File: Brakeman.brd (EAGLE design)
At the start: 37.3 x 48.3 mm, 9 parts

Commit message: added values for connectors
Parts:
- PADL1, PADL2, PADNF2, PADSF2: value (none) -> pad
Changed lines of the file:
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@@
 <attribute name="VALUE" x="18.2626" y="33.655" size="0.0254" layer="28" rot="MR0"/>
 </element>
-<element name="PADL1" library="wirepad" package="SMD1.27-2.54" value="" x="18.2626" y="33.655" smashed="yes">
+<element name="PADL1" library="wirepad" package="SMD1.27-2.54" value="pad" x="18.2626" y="33.655" smashed="yes">
 <attribute name="VALUE" x="18.2626" y="33.655" size="0.0254" layer="27"/>
 </element>
@@
 <attribute name="VALUE" x="5.8166" y="26.162" size="0.0254" layer="28" rot="MR200"/>
 </element>
-<element name="PADL2" library="wirepad" package="SMD1.27-2.54" value="" x="5.8166" y="26.162" smashed="yes" rot="R160">
+<element name="PADL2" library="wirepad" package="SMD1.27-2.54" value="pad" x="5.8166" y="26.162" smashed="yes" rot="R160">
 <attribute name="VALUE" x="5.8166" y="26.162" size="0.0254" layer="27" rot="R160"/>
 </element>
-<element name="PADNF2" library="wirepad" package="SMD1.27-2.54" value="" x="14.859" y="19.9644" smashed="yes" rot="R90">
+<element name="PADNF2" library="wirepad" package="SMD1.27-2.54" value="pad" x="14.859" y="19.9644" smashed="yes" rot="R90">
 <attribute name="VALUE" x="14.859" y="19.9644" size="0.0254" layer="27" rot="R90"/>
 </element>
-<element name="PADSF2" library="wirepad" package="SMD1.27-2.54" value="" x="8.7122" y="19.9898" smashed="yes" rot="R90">
+<element name="PADSF2" library="wirepad" package="SMD1.27-2.54" value="pad" x="8.7122" y="19.9898" smashed="yes" rot="R90">
 <attribute name="VALUE" x="8.7122" y="19.9898" size="0.0254" layer="27" rot="R90"/>
 </element>

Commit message: added values for connectors
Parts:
- PADNA, PADNA2, PADNF, PADSF: value (none) -> pad
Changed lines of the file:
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@@
 <attribute name="VALUE" x="13.4366" y="29.21" size="1.27" layer="28" rot="MR0"/>
 </element>
-<element name="PADNA" library="wirepad" package="SMD1.27-2.54" value="" x="18.2626" y="33.655" smashed="yes" rot="MR0">
+<element name="PADNA" library="wirepad" package="SMD1.27-2.54" value="pad" x="18.2626" y="33.655" smashed="yes" rot="MR0">
 <attribute name="VALUE" x="18.2626" y="33.655" size="0.0254" layer="28" rot="MR0"/>
 </element>
@@
 <attribute name="VALUE" x="18.2626" y="33.655" size="0.0254" layer="27"/>
 </element>
-<element name="PADNA2" library="wirepad" package="SMD1.27-2.54" value="" x="5.8166" y="26.162" smashed="yes" rot="MR200">
+<element name="PADNA2" library="wirepad" package="SMD1.27-2.54" value="pad" x="5.8166" y="26.162" smashed="yes" rot="MR200">
 <attribute name="VALUE" x="5.8166" y="26.162" size="0.0254" layer="28" rot="MR200"/>
 </element>
@@
 <attribute name="VALUE" x="8.7122" y="19.9898" size="0.0254" layer="27" rot="R90"/>
 </element>
-<element name="PADSF" library="wirepad" package="SMD1.27-2.54" value="" x="8.7122" y="19.9644" smashed="yes" rot="MR270">
+<element name="PADSF" library="wirepad" package="SMD1.27-2.54" value="pad" x="8.7122" y="19.9644" smashed="yes" rot="MR270">
 <attribute name="VALUE" x="8.7122" y="19.9644" size="0.0254" layer="28" rot="MR270"/>
 </element>
-<element name="PADNF" library="wirepad" package="SMD1.27-2.54" value="" x="14.8844" y="19.9644" smashed="yes" rot="MR270">
+<element name="PADNF" library="wirepad" package="SMD1.27-2.54" value="pad" x="14.8844" y="19.9644" smashed="yes" rot="MR270">
 <attribute name="VALUE" x="14.8844" y="19.9644" size="0.0254" layer="28" rot="MR270"/>
 </element>

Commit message: Version 2.4
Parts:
- removed PADL1, PADL2, PADNA, PADNA2, PADNF2, PADSF2: pad, wirepad:SMD1.27-2.54
- removed R1: 1k0, resistor:0204/5
- added LED1, LED2: (no value), SPCoast:0603-LED
- added PADNF1, PADSF1: pad, SPCoast:SMD1,27-2,54
- added R1K: 1k0, resistor:R0603
- PADNF, PADSF: device wirepad:SMD1.27-2.54 -> SPCoast:SMD1,27-2,54
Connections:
- net LIMITED: now also LED1.C, LED2.A, R1K.1; no longer PADL1.1, PADL2.1, R1.1
- net N: now also LED1.A, LED2.C, PADNF1.1; no longer PADNA.1, PADNA2.1, PADNF2.1
- net S: now also PADSF1.1, R1K.2; no longer PADSF2.1, R1.2
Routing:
- net N: track 38.6 -> 35.5 mm, vias 2 -> 4
- net LIMITED: track 19.3 -> 21.3 mm
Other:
- board size 37.3 x 48.3 mm -> 23.9 x 45.7 mm
- board text added: "2016.11 2024.01"
- board text added: "John Plocher 2024.01"
- board text added: "Safety Sam DCC Flagman"
- board text removed: "2016.11"
- board text removed: "V-Groove"

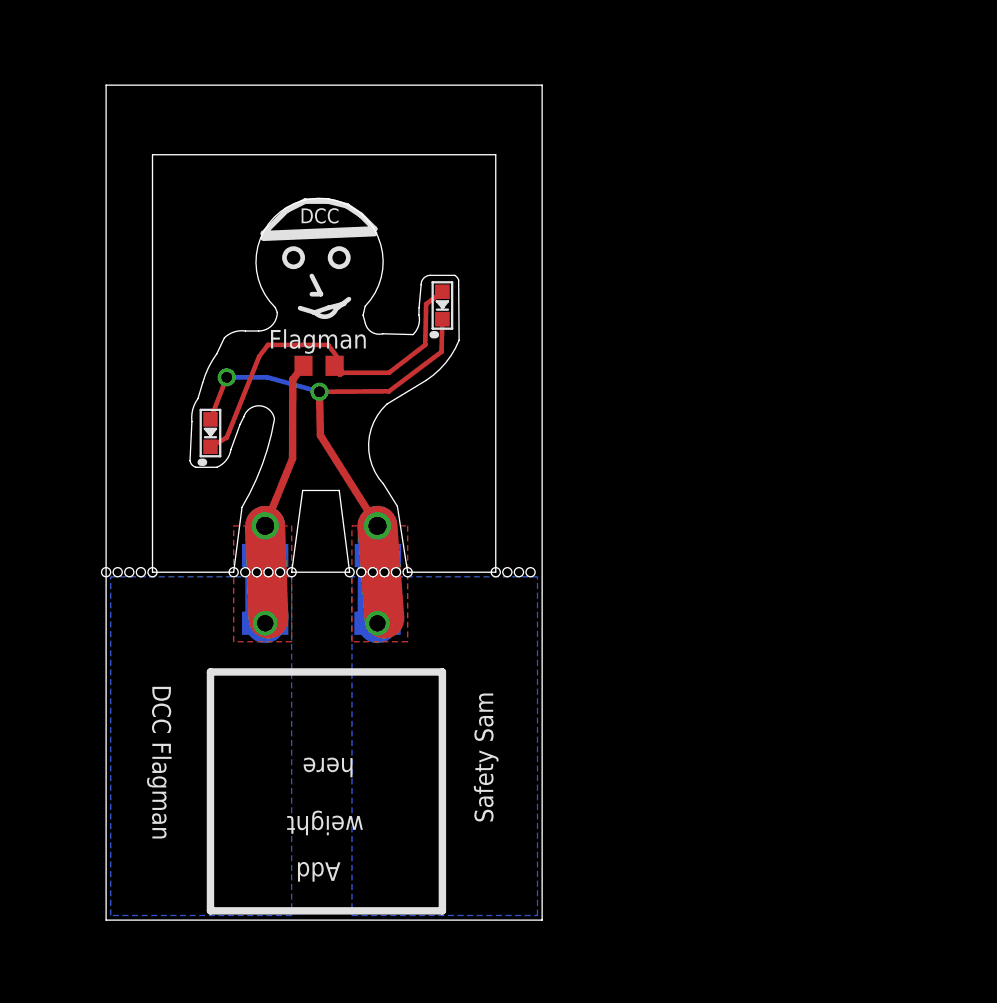
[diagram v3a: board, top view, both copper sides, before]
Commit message: Revert "Version 2.4"
This reverts commit de817f9b6bc09cb4258c25781ce6263bd1cc7bce.
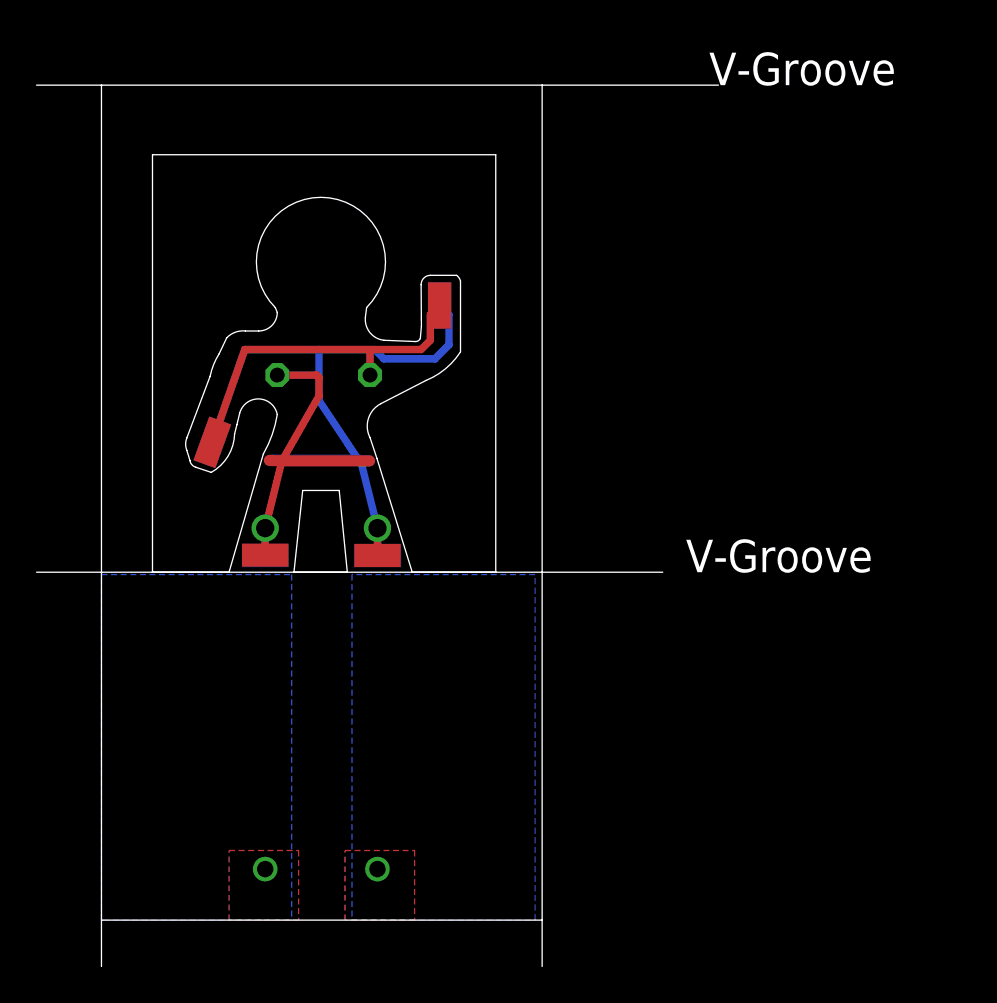
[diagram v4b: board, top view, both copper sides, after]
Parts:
- removed LED1, LED2: (no value), SPCoast:0603-LED
- removed PADNF1, PADSF1: pad, SPCoast:SMD1,27-2,54
- removed R1K: 1k0, resistor:R0603
- added PADL1, PADL2, PADNA, PADNA2, PADNF2, PADSF2: pad, wirepad:SMD1.27-2.54
- added R1: 1k0, resistor:0204/5
- PADNF, PADSF: device SPCoast:SMD1,27-2,54 -> wirepad:SMD1.27-2.54
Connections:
- net LIMITED: now also PADL1.1, PADL2.1, R1.1; no longer LED1.C, LED2.A, R1K.1
- net N: now also PADNA.1, PADNA2.1, PADNF2.1; no longer LED1.A, LED2.C, PADNF1.1
- net S: now also PADSF2.1, R1.2; no longer PADSF1.1, R1K.2
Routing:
- net N: track 35.5 -> 38.6 mm, vias 4 -> 2
- net LIMITED: track 21.3 -> 19.3 mm
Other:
- board size 23.9 x 45.7 mm -> 37.3 x 48.3 mm
- board text added: "2016.11"
- board text added: "V-Groove"
- board text removed: "2016.11 2024.01"
- board text removed: "John Plocher 2024.01"
- board text removed: "Safety Sam DCC Flagman"

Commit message: added foot tiedowns
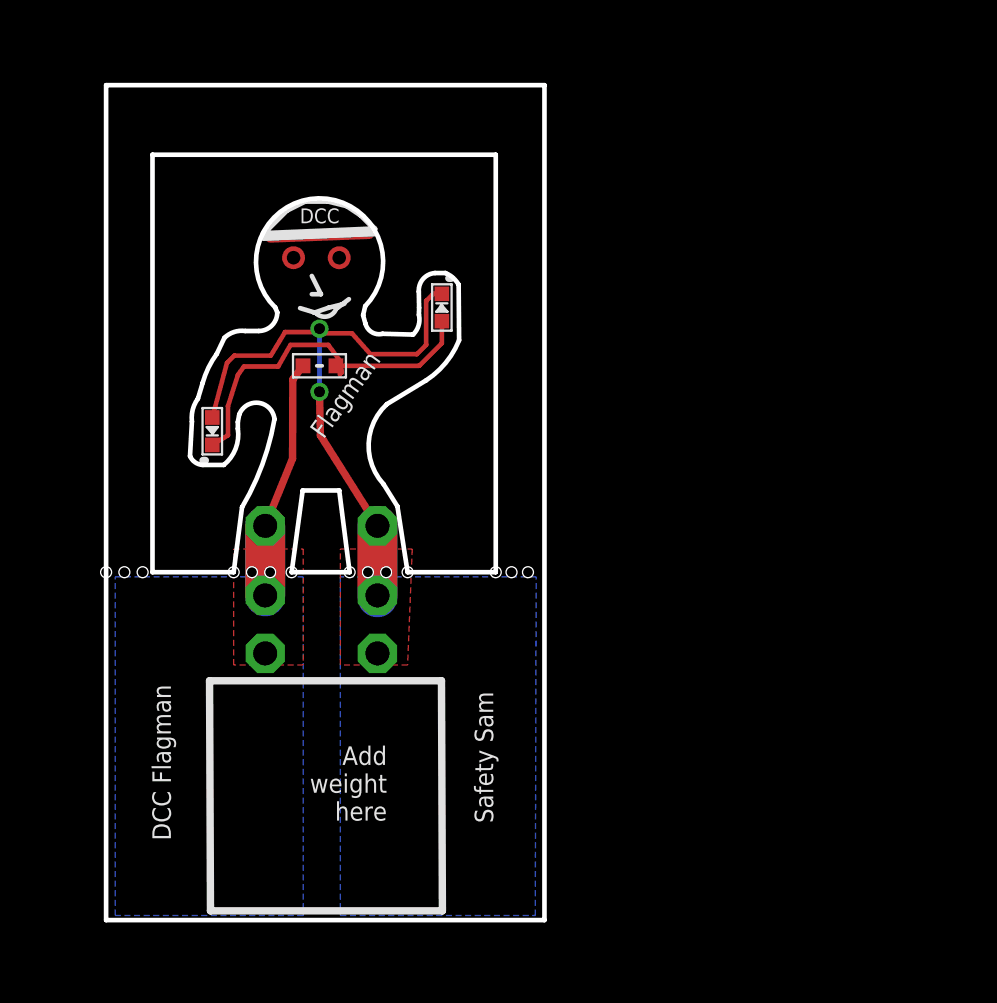
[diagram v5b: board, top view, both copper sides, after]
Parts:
- removed PADL1, PADL2, PADNA, PADNA2, PADNF, PADNF2, PADSF, PADSF2: pad, wirepad:SMD1.27-2.54
- removed R1: 1k0, resistor:0204/5
- added LED1, LED2: R, SPCoast:0603-LED
- added R1K: 1k0, SPCoast:0603-RES
- added TP1, TP2, TP3, TP4, TP5, TP6: PTR1PAD1-13, testpad:P1-13
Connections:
- net LIMITED: now also LED1.C, LED2.A, R1K.1; no longer PADL1.1, PADL2.1, R1.1
- net N: now also LED1.A, LED2.C, TP3.TP, TP4.TP, TP6.TP; no longer PADNA.1, PADNA2.1, PADNF.1, PADNF2.1
- net S: now also R1K.2, TP1.TP, TP2.TP, TP5.TP; no longer PADSF.1, PADSF2.1, R1.2
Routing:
- net S$1: track 0.00 -> 5.40 mm
- net S: track 19.7 -> 16.9 mm, vias 2 -> 0
- net LIMITED: track 19.3 -> 20.1 mm
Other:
- board size 37.3 x 48.3 mm -> 24 x 45.7 mm
- board text added: "2016.11 2024.01"
- board text added: "Add weight here"
- board text added: "John Plocher 2024.01"
- board text added: "Safety Sam DCC Flagman"
- board text removed: "2016.11"
- board text removed: "Add"
- board text removed: "V-Groove"
- board text removed: "here"
- board text removed: "weight"

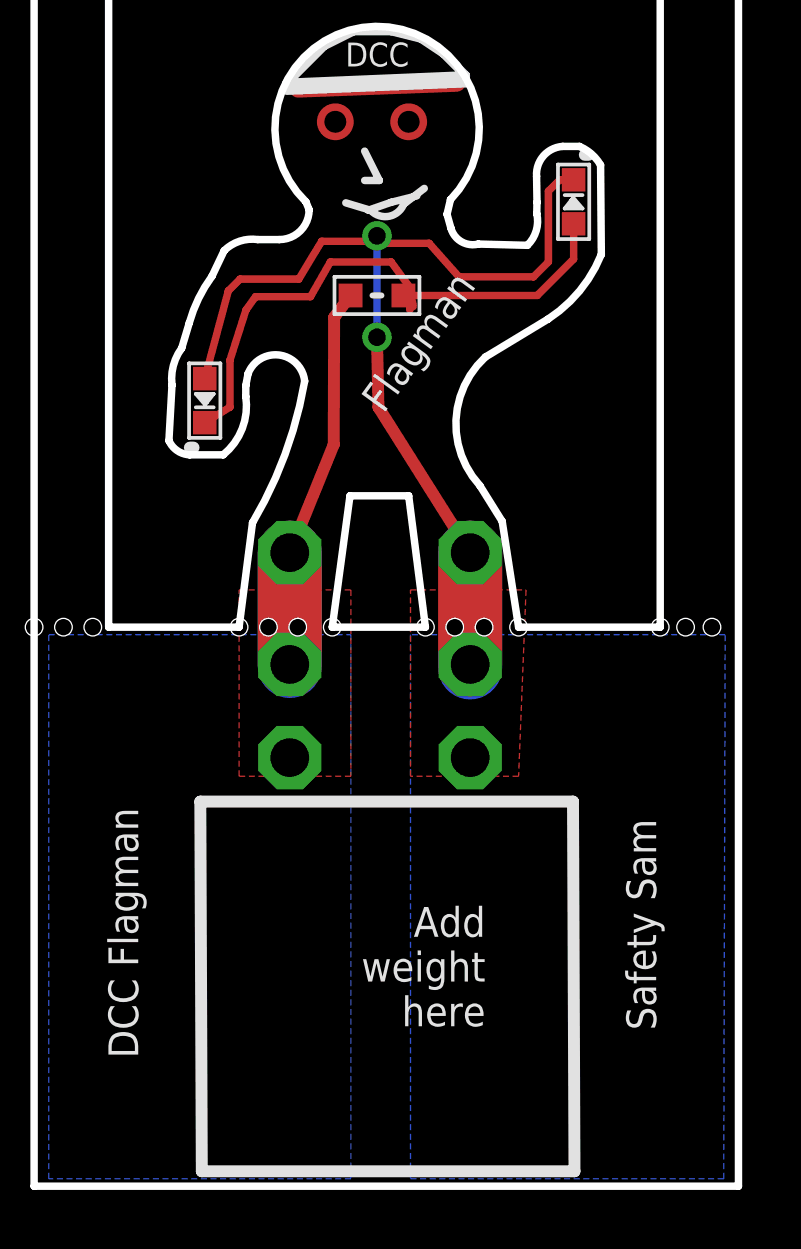
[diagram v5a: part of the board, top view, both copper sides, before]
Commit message: fixed silkscreen/layer issues with PCBWay
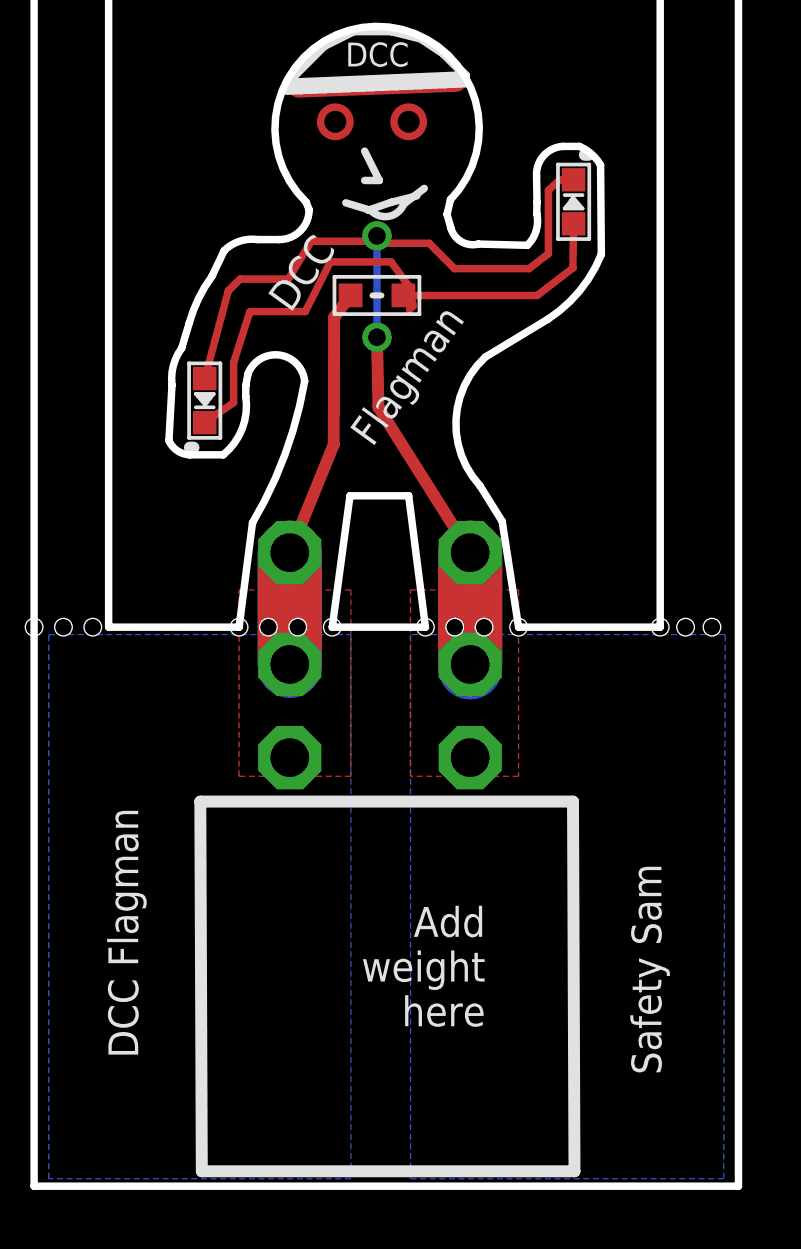
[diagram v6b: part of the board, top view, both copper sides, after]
